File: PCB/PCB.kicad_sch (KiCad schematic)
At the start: 17 parts, among them J1 Conn_01x06_Female, J3 DB25_Receptacle_MountingHoles, U13 74HC165, U15 LT3042xMSE, U16 74HC165

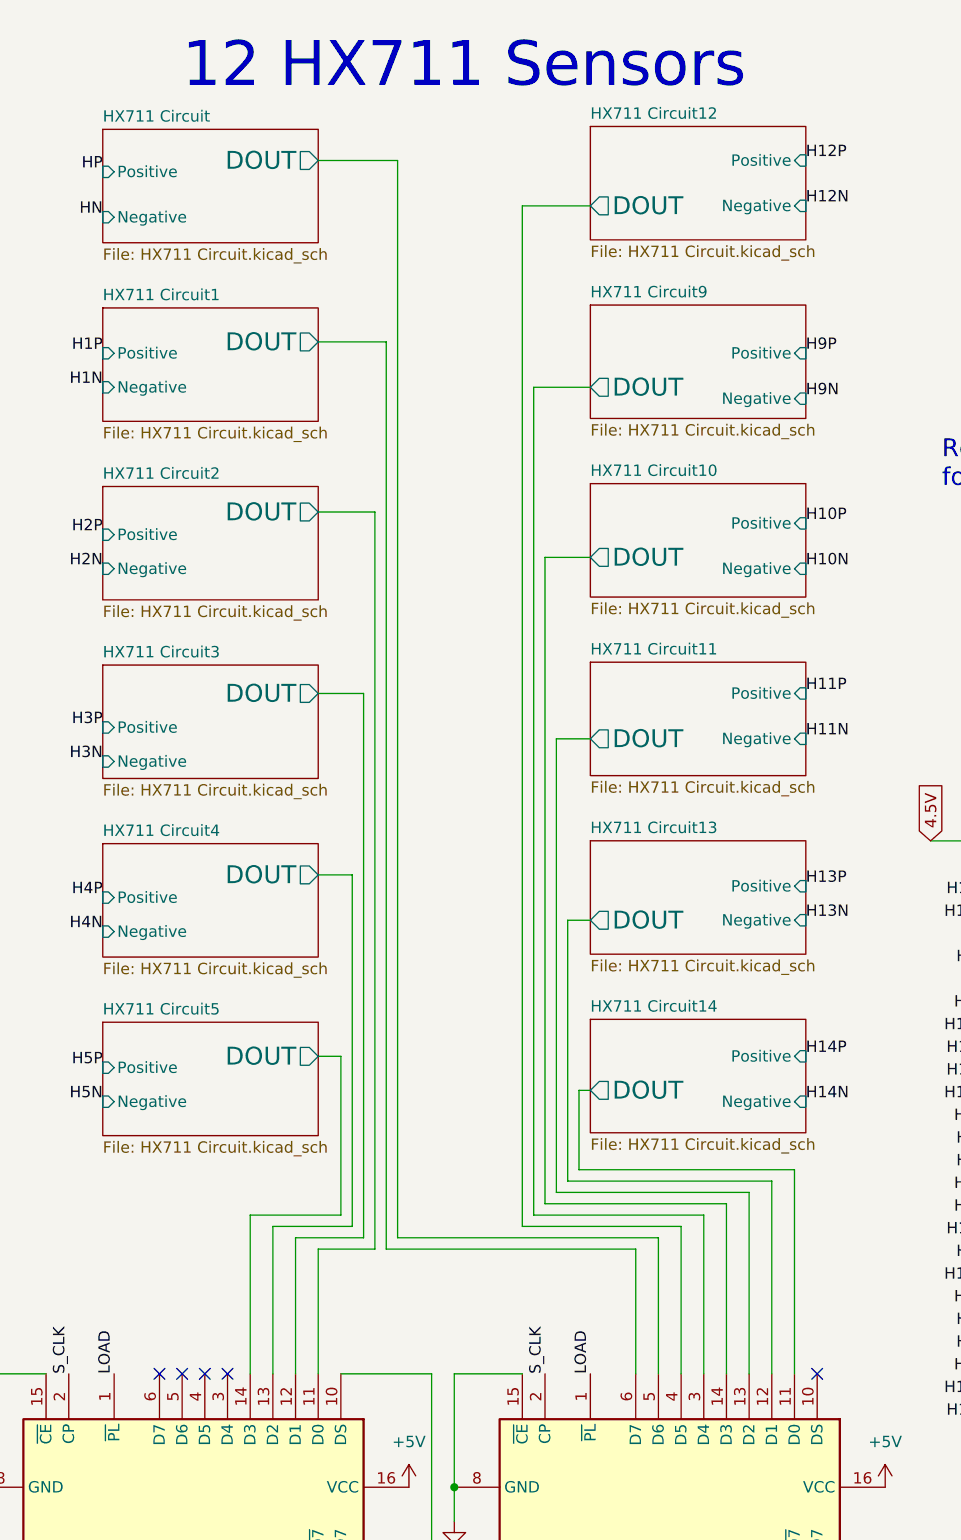
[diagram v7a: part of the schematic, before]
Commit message: Final Radial version
Solved a lot of problems, but restarting.
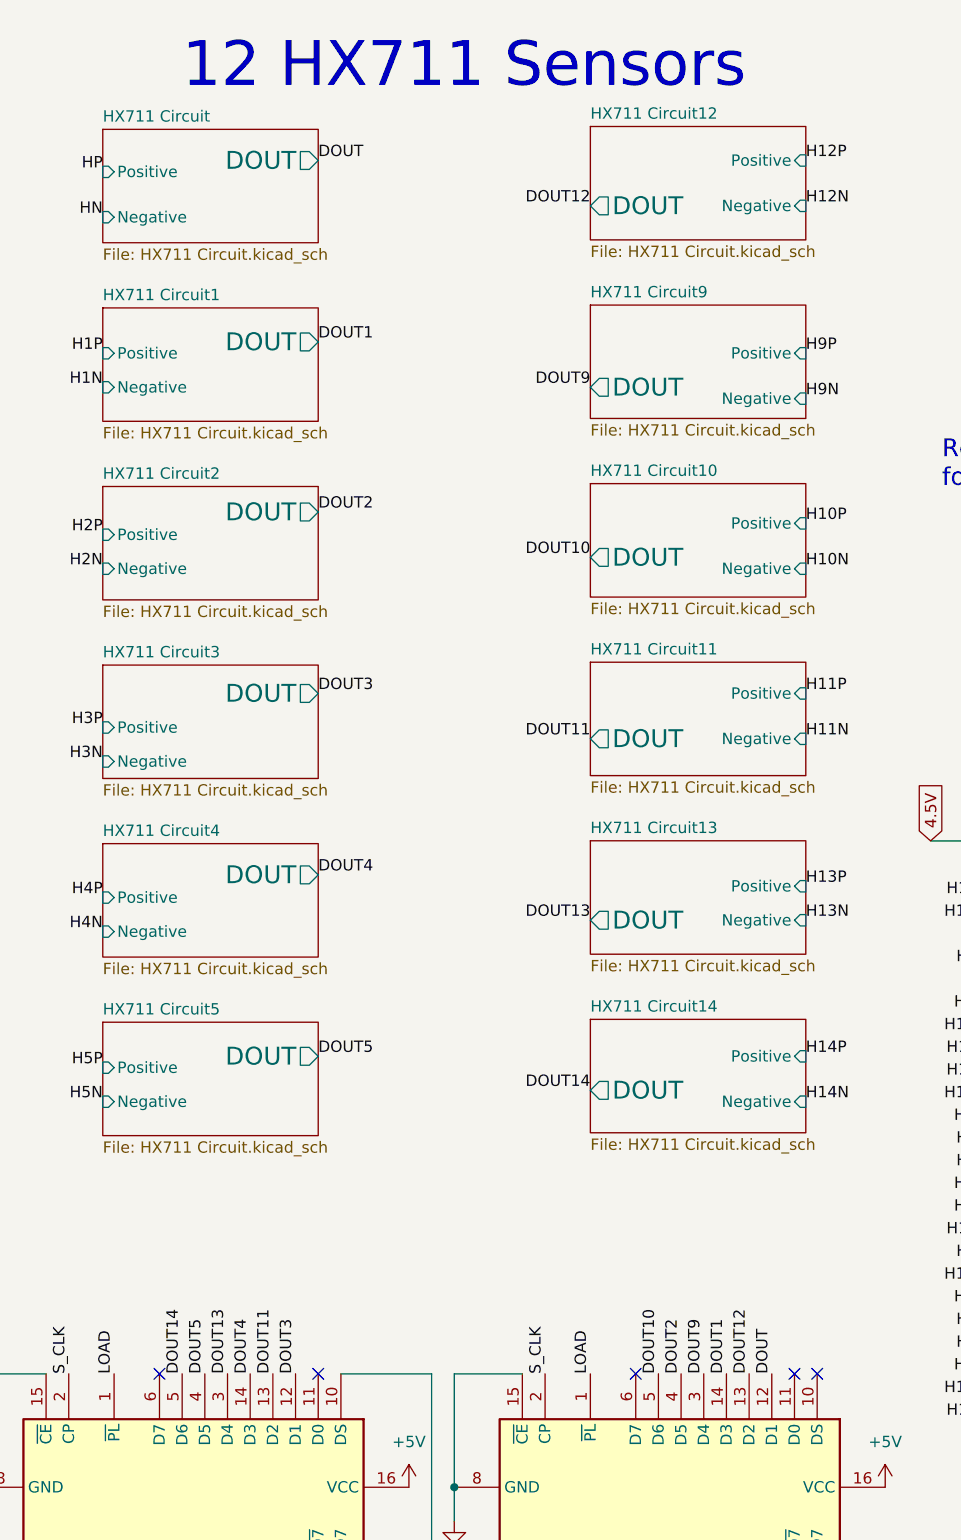
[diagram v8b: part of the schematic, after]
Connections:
- net DOUT13: now reaches U13.3 (D4)
- net DOUT5: now reaches U13.4 (D5)
- net DOUT14: now reaches U13.5 (D6)
- net HX711 Circuit/DOUT renamed DOUT10
- net HX711 Circuit1/DOUT: no longer names the net of U16.6 (D7)
- net HX711 Circuit10/DOUT renamed DOUT1
- net HX711 Circuit11/DOUT renamed DOUT12
- net HX711 Circuit12/DOUT renamed DOUT2
- net HX711 Circuit13/DOUT renamed DOUT
- net HX711 Circuit14/DOUT: no longer names the net of U16.11 (D0)
- net HX711 Circuit2/DOUT: no longer names the net of U13.11 (D0)
- net HX711 Circuit3/DOUT renamed DOUT3
- net HX711 Circuit4/DOUT renamed DOUT11
- net HX711 Circuit5/DOUT renamed DOUT4
- net HX711 Circuit9/DOUT renamed DOUT9
